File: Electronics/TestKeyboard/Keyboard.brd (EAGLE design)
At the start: 157.5 x 59.7 mm, 69 parts

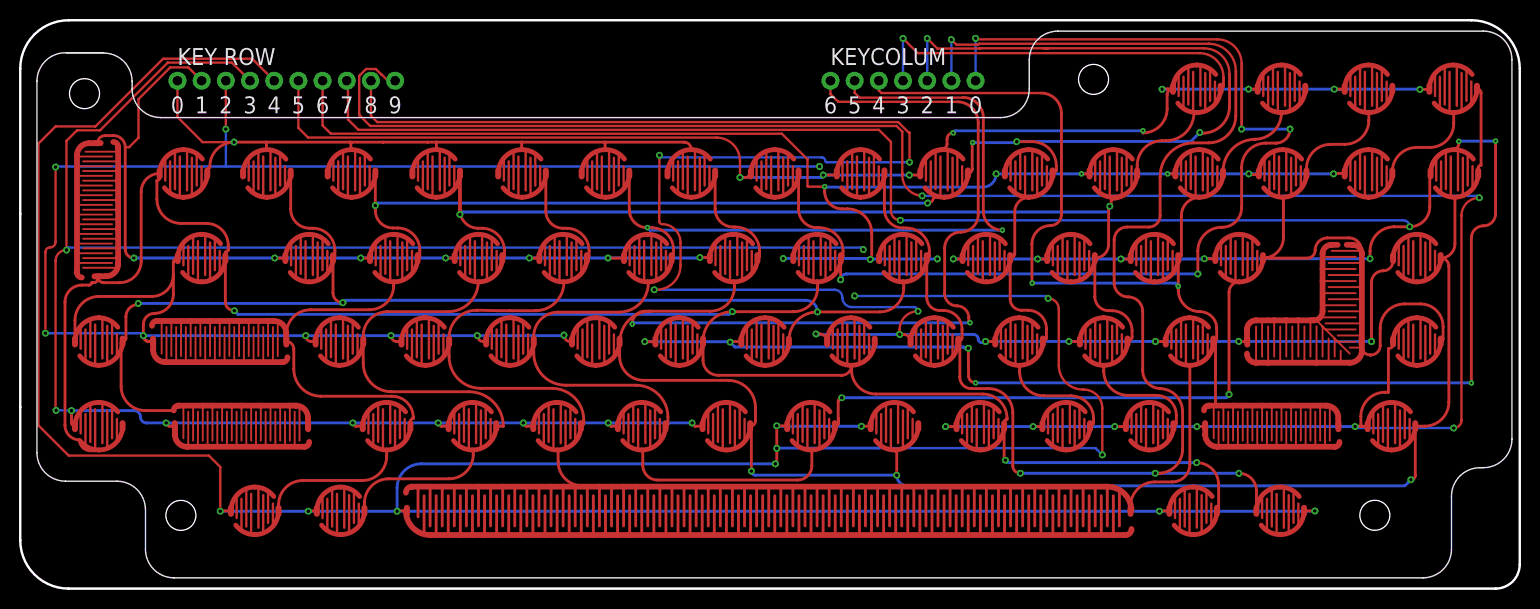
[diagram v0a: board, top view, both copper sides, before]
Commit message: fixed test keyboard
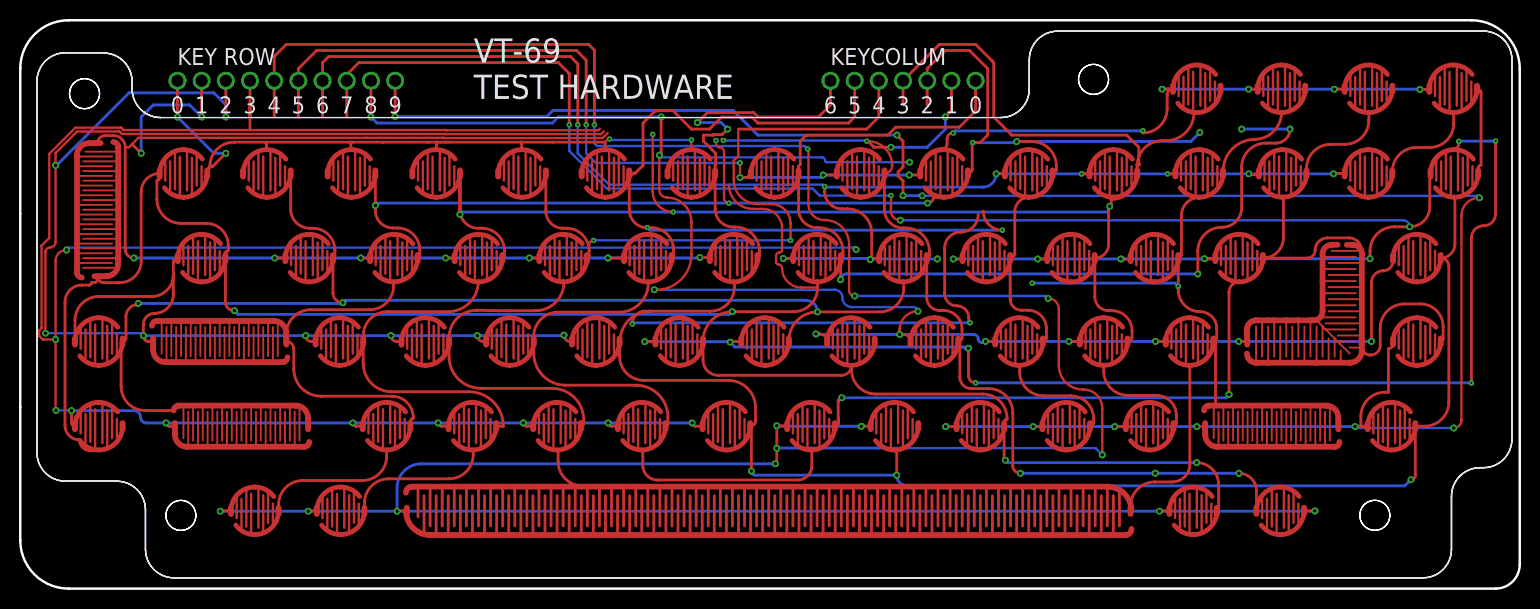
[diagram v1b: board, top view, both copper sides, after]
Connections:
- removed net KEYCOLUM0: K_7.P$2, K_<.P$2, K_ESC.P$2, K_G.P$2, K_J.P$2, K_NOSCL.P$2, K_RIGHTALT.P$2, K_SETUP.P$2, K_TAB.P$2, K_U.P$2
- removed net KEYCOLUM1: K-1.P$2, K_8.P$2, K_CAPS.P$2, K_H.P$2, K_I.P$2, K_K.P$2, K_LSHIFT.P$2, K_Q.P$2, K_RIGHTMETA.P$2
- removed net KEYCOLUM2: K-2.P$2, K_0.P$2, K_9.P$2, K_>.P$2, K_CONTROL.P$2, K_L.P$2, K_LEFTMETA.P$2, K_O.P$2, K_W.P$2, K_Z.P$2
- removed net KEYCOLUM3: K_3.P$2, K_?.P$2, K_A.P$2, K_E.P$2, K_LEFT.P$2, K_LEFTALT.P$2, K_P.P$2, K_SEMI.P$2, K_USCORE.P$2, K_X.P$2
- removed net KEYCOLUM4: K_4.P$2, K_C.P$2, K_DOWN.P$2, K_PLUS.P$2, K_QUOTE.P$2, K_R.P$2, K_RSHIFT.P$2, K_S.P$2, K_SPACE.P$2, K_{.P$2
- removed net KEYCOLUM5: K-5.P$2, K_D.P$2, K_N.P$2, K_PIPE.P$2, K_RETURN.P$2, K_T.P$2, K_TILDE.P$2, K_UP.P$2, K_V.P$2, K_}.P$2
- removed net KEYCOLUM6: K_6.P$2, K_B.P$2, K_BACK.P$2, K_BREAK.P$2, K_DEL.P$2, K_F.P$2, K_LINE.P$2, K_M.P$2, K_RIGHT.P$2, K_Y.P$2
- removed net KEYROW0: K-1.P$1, K-2.P$1, K-5.P$1, K_3.P$1, K_4.P$1, K_6.P$1, K_ESC.P$1
- removed net KEYROW1: K_E.P$1, K_Q.P$1, K_R.P$1, K_SETUP.P$1, K_T.P$1, K_W.P$1, K_Y.P$1
- removed net KEYROW2: K_A.P$1, K_CAPS.P$1, K_CONTROL.P$1, K_D.P$1, K_F.P$1, K_S.P$1, K_TAB.P$1
- removed net KEYROW3: K_B.P$1, K_C.P$1, K_LSHIFT.P$1, K_NOSCL.P$1, K_V.P$1, K_X.P$1, K_Z.P$1
- removed net KEYROW4: K_LEFTALT.P$1, K_LEFTMETA.P$1, K_M.P$1, K_N.P$1, K_RIGHTALT.P$1, K_RIGHTMETA.P$1, K_SPACE.P$1
- removed net KEYROW5: K_7.P$1, K_8.P$1, K_9.P$1, K_DOWN.P$1, K_LEFT.P$1, K_RIGHT.P$1, K_UP.P$1
- removed net KEYROW6: K_0.P$1, K_BACK.P$1, K_I.P$1, K_PLUS.P$1, K_TILDE.P$1, K_U.P$1, K_USCORE.P$1
- removed net KEYROW7: K_BREAK.P$1, K_G.P$1, K_H.P$1, K_O.P$1, K_P.P$1, K_{.P$1, K_}.P$1
- removed net KEYROW8: K_DEL.P$1, K_J.P$1, K_K.P$1, K_L.P$1, K_QUOTE.P$1, K_RETURN.P$1, K_SEMI.P$1
- removed net KEYROW9: K_<.P$1, K_>.P$1, K_?.P$1, K_LINE.P$1, K_PIPE.P$1, K_RSHIFT.P$1
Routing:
- net KEYCOLUM1: track 296.4 -> 241.2 mm, vias 8 -> 11
- net KEYROW1: track 96.6 -> 149.8 mm, vias 8 -> 10
- net KEYROW3: track 212.4 -> 263.7 mm, vias 11 -> 12
- net KEYROW8: track 214.5 -> 190.3 mm, vias 12 -> 14
- net KEYCOLUM2: track 250.2 -> 232.4 mm, vias 7 -> 8
- net KEYCOLUM4: track 249.3 -> 265.3 mm, vias 3 -> 5
- net KEYROW6: track 146.1 -> 159.3 mm, vias 10 -> 11
- net KEYROW0: track 88.9 -> 100.3 mm, vias 2 -> 5
- net KEYROW5: track 139.7 -> 149.6 mm, vias 10 -> 12
- net KEYCOLUM5: track 270.4 -> 279.6 mm
- net KEYCOLUM3: track 232.4 -> 239.7 mm, vias 4 -> 5
- net KEYROW9: track 228.2 -> 221.1 mm, vias 9 -> 12
- net KEYROW4: track 337.1 -> 343.2 mm, vias 13 -> 15
- net KEYROW7: track 312.9 -> 318.0 mm, vias 15 -> 17
- net KEYCOLUM0: track 328.4 -> 331.6 mm, vias 10 -> 9
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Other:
- board text added: "PENIS"
- board text added: "VT-69 TEST HARDWARE"
